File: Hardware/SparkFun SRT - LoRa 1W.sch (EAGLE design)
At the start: 56 parts, among them J1 QWIIC_RIGHT_ANGLE, J3 USB C, J4 JTAG, U2 ATSAMD21G-A, U3 AP2112K-3.3, U4 E19-915M30S, Y1 32.768kHz

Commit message: Add ignore. Fix RP-SMA connector.
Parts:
- removed E1: SMA, SparkFun-RF:ANTENNA-SMA-GROUNDEDEDGE_SMA
- added E2: RP-SMA, SparkFun-RF:ANTENNA-SMA-GROUNDEDEDGE_RPSMA
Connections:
- net GND: now also E2.GND; no longer E1.GND
- net LORA_ANT: now also E2.SIGNAL; no longer E1.SIGNAL

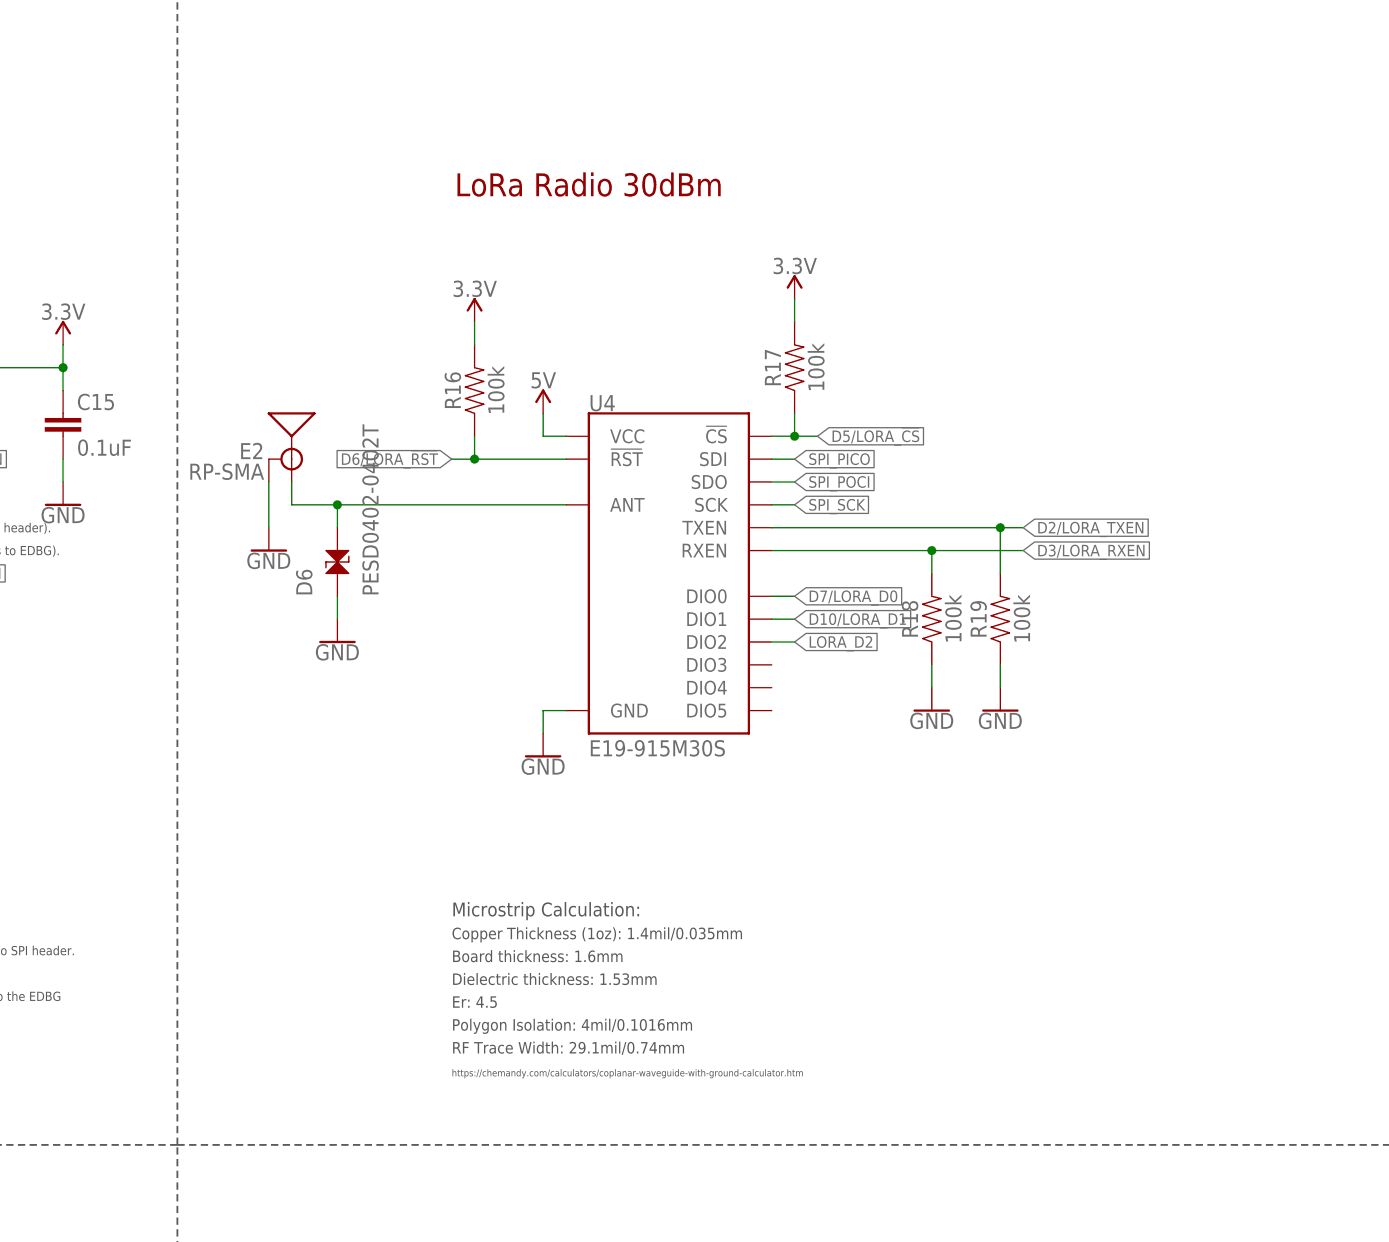
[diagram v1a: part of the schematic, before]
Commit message: Update to new RP SMA connector package
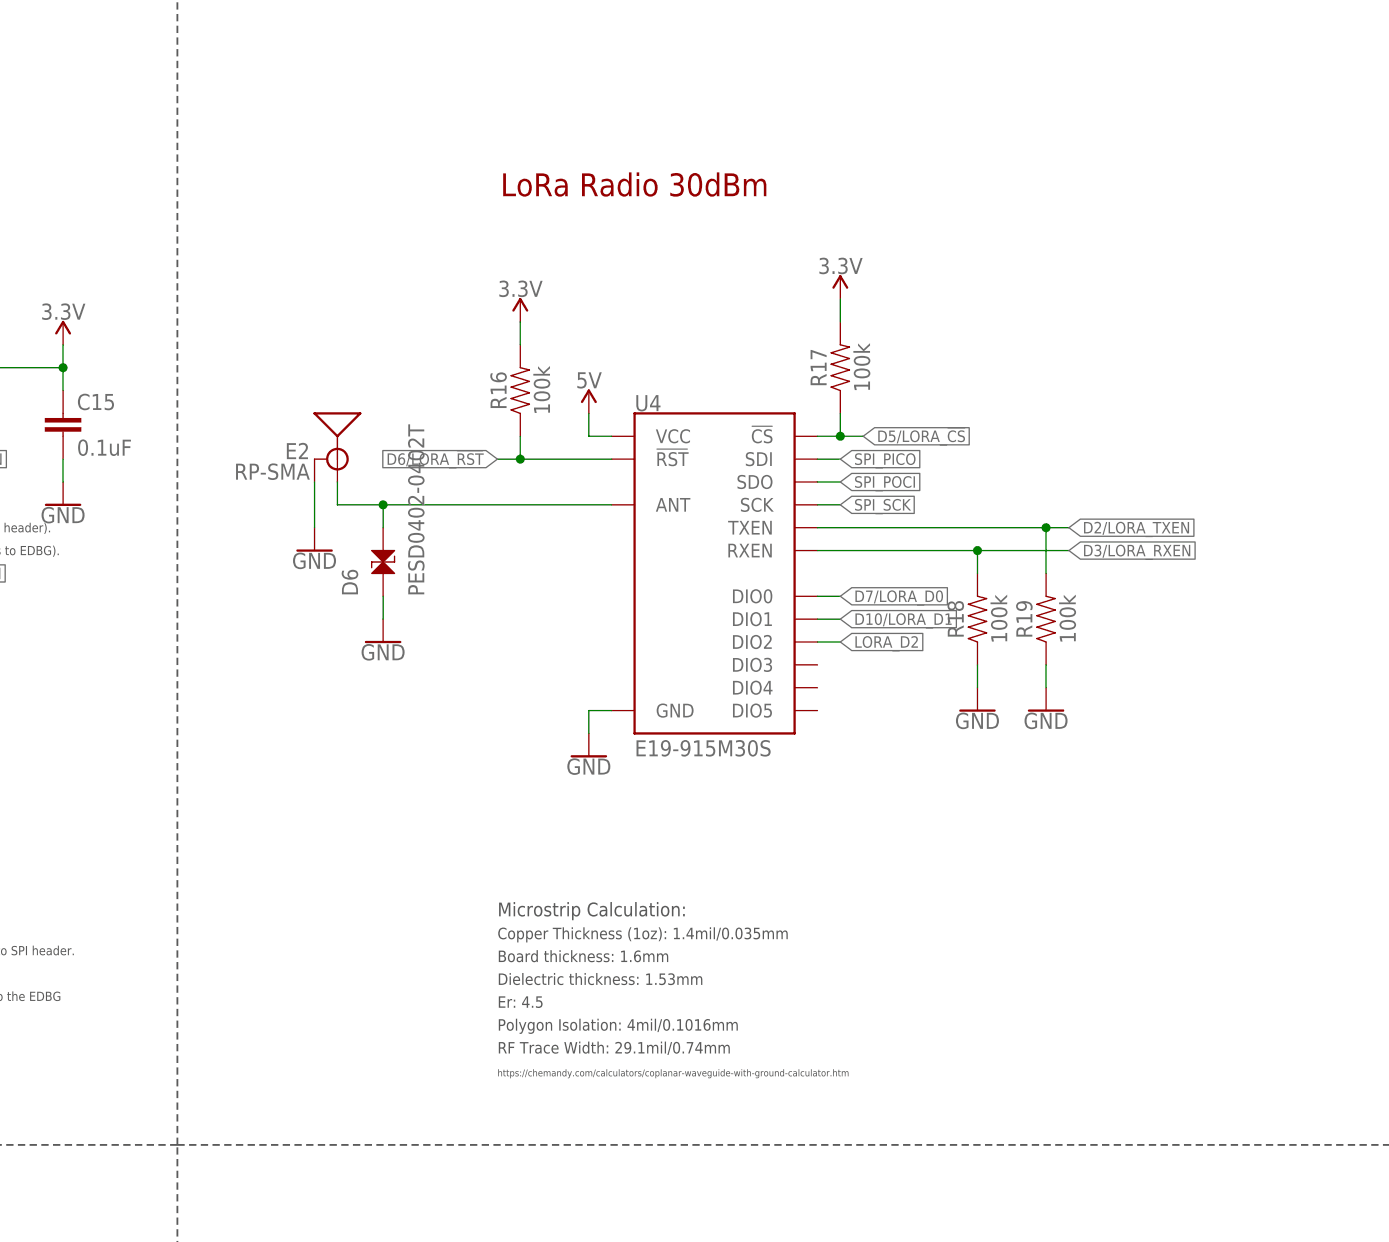
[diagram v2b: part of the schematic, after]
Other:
- moved on the sheet: D6, E2, R16, R17, R18, R19, U4
